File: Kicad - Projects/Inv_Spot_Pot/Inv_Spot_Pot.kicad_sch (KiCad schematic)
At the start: 72 parts, among them J1 Screw_Terminal_01x03, J2 PWM, J3 Display_Power, J4 Current_Sense, J5 PWM, Q1 40T120, Q2 40T120, Q3 40T120, Q4 40T120, T1 Transformer_1P_1S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

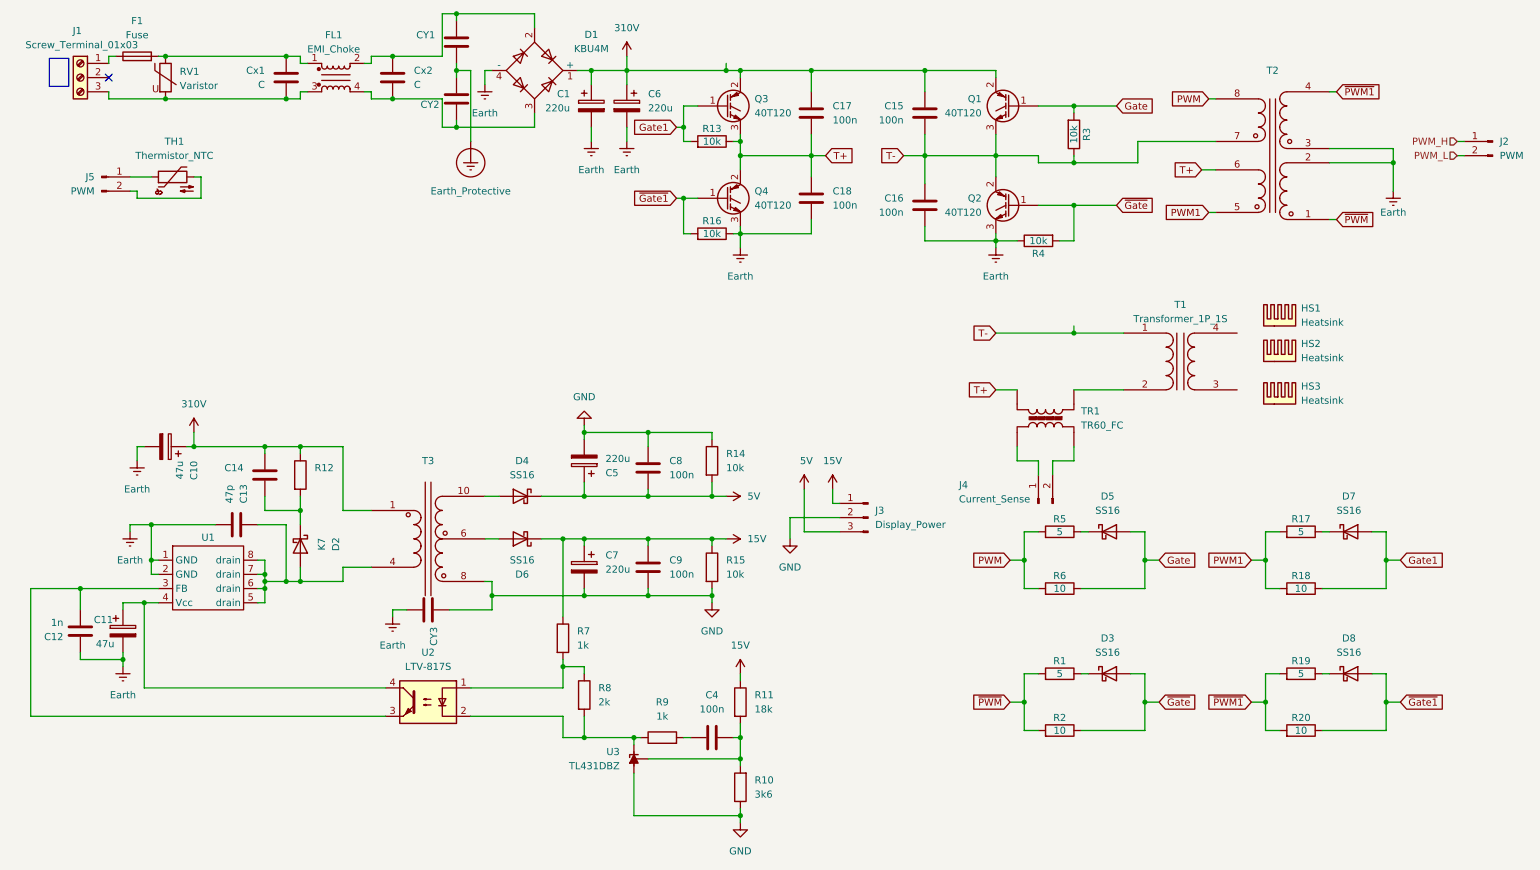
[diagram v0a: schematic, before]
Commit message: Ajustes Finais
Ajustes finais de footprints e layouts
Considerando aumentar isolamento da trilha T- do IGBT Q2
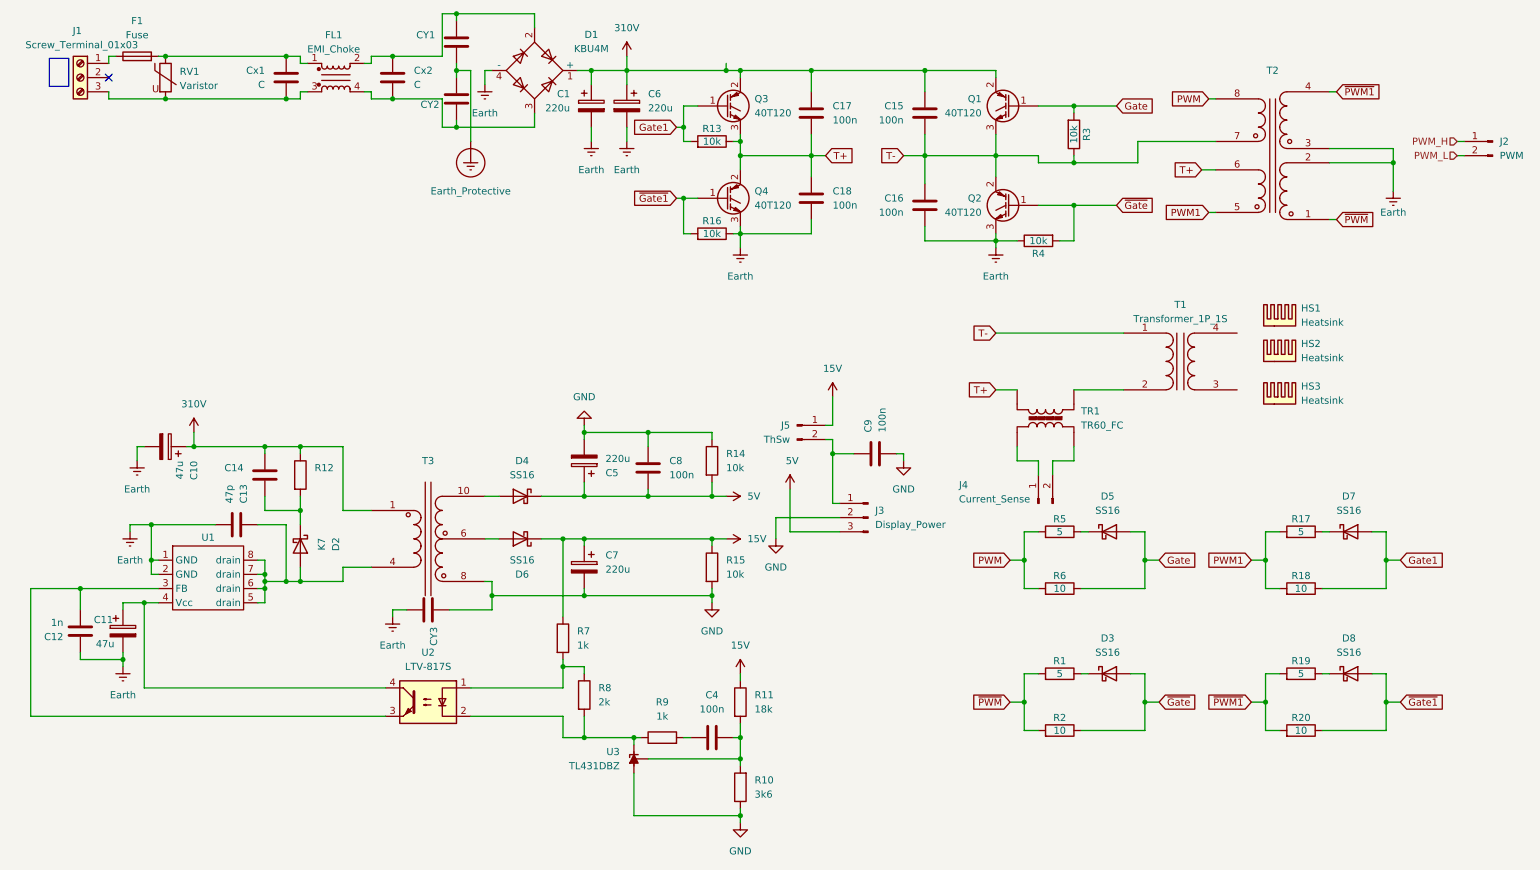
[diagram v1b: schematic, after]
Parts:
- removed TH1: Thermistor_NTC, Resistor_THT:R_Axial_DIN0204_L3.6mm_D1.6mm_P1.90mm_Vertical, symbol Device:Thermistor_NTC
- C1, C6: footprint Capacitor_THT:C_Radial_D16.0mm_H25.0mm_P7.50mm -> Capacitor_THT:CP_Radial_D35.0mm_P10.00mm_SnapIn
- J2, J4: footprint Connector_PinHeader_2.00mm:PinHeader_1x02_P2.00mm_Vertical -> Connector_PinHeader_2.54mm:PinHeader_1x02_P2.54mm_Vertical
- J3: footprint Connector_PinHeader_2.00mm:PinHeader_1x03_P2.00mm_Vertical -> Connector_PinHeader_2.54mm:PinHeader_1x03_P2.54mm_Vertical
- J5: value PWM -> ThSw; footprint Connector_PinHeader_2.00mm:PinHeader_1x02_P2.00mm_Vertical -> Connector_PinHeader_2.54mm:PinHeader_1x02_P2.54mm_Vertical
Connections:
- net 15V: now also J5.1 (Pin_1); no longer C9.1, J3.1 (Pin_1)
- net at J5.2 (Pin_2): now also C9.1, J3.1 (Pin_1)
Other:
- moved on the sheet: C9, J5

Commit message: Ajustes Finais
Ajustes Finais do código, esquemáticos e layouts

Ainda faltam ajustes finos
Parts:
- added R21: 200k, Resistor_SMD:R_1206_3216Metric_Pad1.30x1.75mm_HandSolder, symbol Device:R
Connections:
- net 310V: now also R21.1
- net Earth: now also R21.2
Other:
- moved on the sheet: C15, C16, C17, C18, J2, Q1, Q2, Q3, Q4, R13, R16, R3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

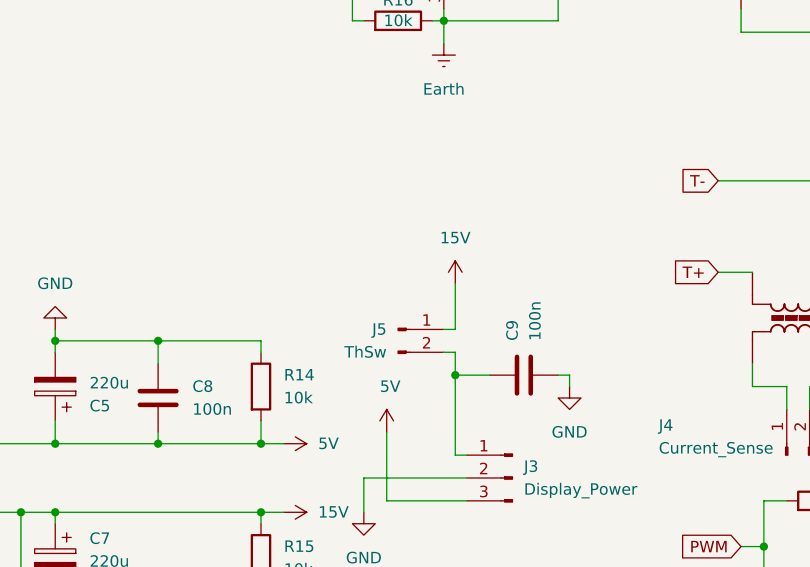
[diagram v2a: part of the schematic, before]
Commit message: Ajustes de Esquemático / Layout
Ajustado símbolo da chave bimetálica na linha de 15V para proteção térmica

Ajustada trilhas de PWM que estavam sendo cobertas por um capacitor
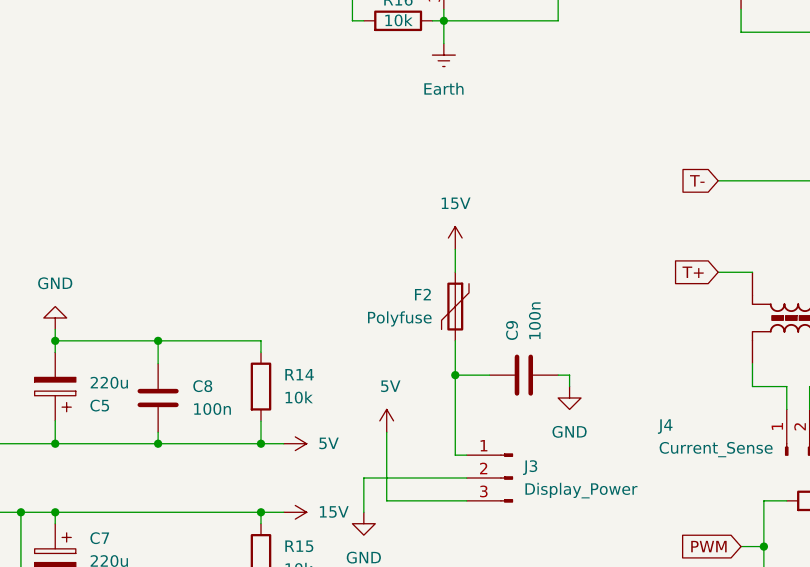
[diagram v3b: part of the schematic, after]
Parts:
- removed J5: ThSw, Connector_PinHeader_2.54mm:PinHeader_1x02_P2.54mm_Vertical, symbol Connector:Conn_01x02_Pin
- added F2: Polyfuse, Connector_PinHeader_2.54mm:PinHeader_1x02_P2.54mm_Vertical, symbol Device:Polyfuse
- F1: footprint Fuse:Fuseholder_Clip-5x20mm_Bel_FC-203-22_Lateral_P17.80x5.00mm_D1.17mm_Horizontal -> Fuse:Fuseholder_Clip-5x20mm_Schurter_CQM_Inline_P20.60x5.00mm_D1.00mm_Horizontal
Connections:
- net 15V: now also F2.1
- net at C9.1, J3.1 (Pin_1): now also F2.2
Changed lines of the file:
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@@
 	)
 	(junction
-		(at 160.02 102.87)
-		(diameter 0)
-		(color 0 0 0 0)
-	)
-	(junction
 		(at 81.28 31.75)
 		(diameter 0)
@@
 	)
 	(junction
+		(at 160.02 102.87)
+		(diameter 0)
+		(color 0 0 0 0)
+	)
+	(junction
 		(at 115.57 99.06)
 		(diameter 0)
@@
 	(wire
 		(pts
-			(xy 158.75 97.79) (xy 160.02 97.79)
-		)
-		(stroke
-			(width 0)
-			(type default)
-		)
-	)
-	(wire
-		(pts
 			(xy 127 157.48) (xy 143.51 157.48)
 		)
@@
 	(wire
 		(pts
-			(xy 160.02 100.33) (xy 160.02 102.87)
-		)
-		(stroke
-			(width 0)
-			(type default)
-		)
-	)
-	(wire
-		(pts
 			(xy 92.71 33.02) (xy 92.71 34.29)
 		)
@@
 	(wire
 		(pts
-			(xy 160.02 92.71) (xy 160.02 97.79)
+			(xy 160.02 88.9) (xy 160.02 91.44)
 		)
 		(stroke
@@
 	(wire
 		(pts
-			(xy 158.75 100.33) (xy 160.02 100.33)
-		)
-		(stroke
-			(width 0)
-			(type default)
-		)
-	)
-	(wire
-		(pts
 			(xy 204.47 49.53) (xy 204.47 53.34)
 		)
@@
 	(wire
 		(pts
+			(xy 160.02 99.06) (xy 160.02 102.87)
+		)
+		(stroke
+			(width 0)
+			(type default)
+		)
+	)
+	(wire
+		(pts
 			(xy 138.43 100.33) (xy 138.43 99.06)
 		)
@@
 	)
 	(symbol
+		(lib_id "Device:Polyfuse")
+		(at 160.02 95.25 0)
+		(mirror y)
+		(unit 1)
+		(body_style 1)
+		(exclude_from_sim no)
+		(in_bom yes)
+		(on_board yes)
+		(in_pos_files yes)
+		(dnp no)
+		(property "Reference" "F2"
+			(at 157.48 93.9799 0)
+			(show_name no)
+			(do_not_autoplace no)
+			(effects
+				(font
+					(size 1.27 1.27)
+				)
+				(justify left)
+			)
+		)
+		(property "Value" "Polyfuse"
+			(at 157.48 96.5199 0)
+			(show_name no)
+			(do_not_autoplace no)
+			(effects
+				(font
+					(size 1.27 1.27)
+				)
+				(justify left)
+			)
+		)
+		(property "Footprint" "Connector_PinHeader_2.54mm:PinHeader_1x02_P2.54mm_Vertical"
+			(at 158.75 100.33 0)
+			(hide yes)
+			(show_name no)
+			(do_not_autoplace no)
+			(effects
+				(font
+					(size 1.27 1.27)
+				)
+				(justify left)
+			)
+		)
+		(property "Datasheet" ""
+			(at 160.02 95.25 0)
+			(hide yes)
+			(show_name no)
+			(do_not_autoplace no)
+			(effects
+				(font
+					(size 1.27 1.27)
+				)
+			)
+		)
+		(property "Description" "Resettable fuse, polymeric positive temperature coefficient"
+			(at 160.02 95.25 0)
+			(hide yes)
+			(show_name no)
+			(do_not_autoplace no)
+			(effects
+				(font
+					(size 1.27 1.27)
+				)
+			)
+		)
+		(pin "1"
+		)
+		(pin "2"
+		)
+		(instances
+			(project "Inv_Spot_Pot"
+				(path "/e27abe51-96c0-4fdf-ba00-b5a281cd0e9c"
+					(reference "F2")
+					(unit 1)
+				)
+			)
+		)
+	)
+	(symbol
 		(lib_id "Device:C")
 		(at 81.28 35.56 0)
@@
 			)
 		)
-		(property "Footprint" "Fuse:Fuseholder_Clip-5x20mm_Bel_FC-203-22_Lateral_P17.80x5.00mm_D1.17mm_Horizontal"
+		(property "Footprint" "Fuse:Fuseholder_Clip-5x20mm_Schurter_CQM_Inline_P20.60x5.00mm_D1.00mm_Horizontal"
 			(at 35.56 33.528 90)
 			(hide yes)
@@
 	(symbol
 		(lib_id "power:VCC")
-		(at 160.02 92.71 0)
+		(at 160.02 88.9 0)
 		(unit 1)
 		(body_style 1)
@@
 		(fields_autoplaced yes)
 		(property "Reference" "#PWR018"
-			(at 160.02 96.52 0)
+			(at 160.02 92.71 0)
 			(hide yes)
 			(show_name no)
@@
 		)
 		(property "Value" "15V"
-			(at 160.02 87.63 0)
+			(at 160.02 83.82 0)
 			(show_name no)
 			(do_not_autoplace no)
@@
 		)
 		(property "Footprint" ""
-			(at 160.02 92.71 0)
+			(at 160.02 88.9 0)
 			(hide yes)
 			(show_name no)
@@
 		)
 		(property "Datasheet" ""
-			(at 160.02 92.71 0)
+			(at 160.02 88.9 0)
 			(hide yes)
 			(show_name no)
@@
 		)
 		(property "Description" "Power symbol creates a global label with name \"VCC\""
-			(at 160.02 92.71 0)
+			(at 160.02 88.9 0)
 			(hide yes)
 			(show_name no)
@@
 					(unit 1)
 				)
-			)
-		)
-	)
-	(symbol
-		(lib_id "Connector:Conn_01x02_Pin")
-		(at 153.67 97.79 0)
-		(unit 1)
-		(body_style 1)
-		(exclude_from_sim no)
-		(in_bom yes)
-		(on_board yes)
-		(in_pos_files yes)
-		(dnp no)
-		(property "Reference" "J5"
-			(at 152.4 97.7899 0)
-			(show_name no)
-			(do_not_autoplace no)
-			(effects
-				(font
-					(size 1.27 1.27)
-				)
-				(justify right)
-			)
-		)
-		(property "Value" "ThSw"
-			(at 152.4 100.3299 0)
-			(show_name no)
-			(do_not_autoplace no)
-			(effects
-				(font
-					(size 1.27 1.27)
-				)
-				(justify right)
-			)
-		)
-		(property "Footprint" "Connector_PinHeader_2.54mm:PinHeader_1x02_P2.54mm_Vertical"
-			(at 153.67 97.79 0)
-			(hide yes)
-			(show_name no)
-			(do_not_autoplace no)
-			(effects
-				(font
-					(size 1.27 1.27)
-				)
-			)
-		)
-		(property "Datasheet" ""
-			(at 153.67 97.79 0)
-			(hide yes)
-			(show_name no)
-			(do_not_autoplace no)
-			(effects
-				(font
-					(size 1.27 1.27)
-				)
-			)
-		)
-		(property "Description" "Generic connector, single row, 01x02, script generated"
-			(at 153.67 97.79 0)
-			(hide yes)
-			(show_name no)
-			(do_not_autoplace no)
-			(effects
-				(font
-					(size 1.27 1.27)
-				)
-			)
-		)
-		(pin "2"
-		)
-		(pin "1"
-		)
-		(instances
-			(project "Inv_Spot_Pot"
-				(path "/e27abe51-96c0-4fdf-ba00-b5a281cd0e9c"
-					(reference "J5")
-					(unit 1)
-				)

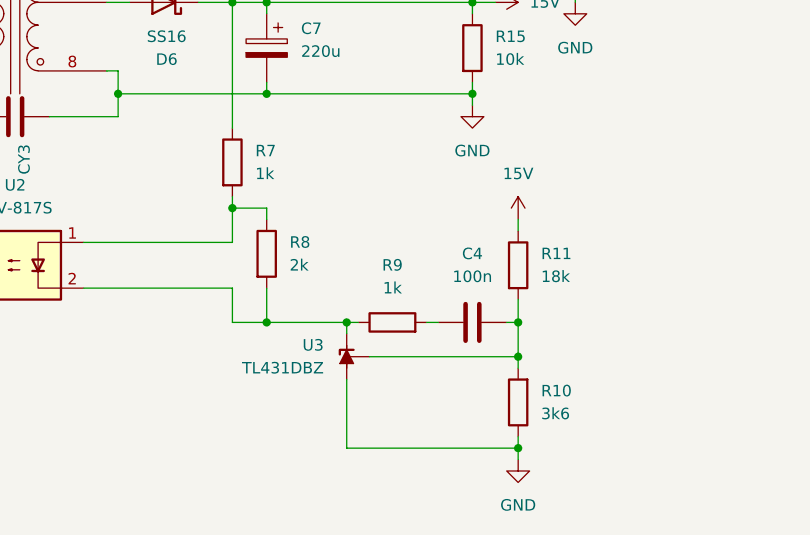
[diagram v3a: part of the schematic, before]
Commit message: Melhora no Acionamento do Trigger
Acionamento do trigger agora ocorre quando o circuito é fechado, não aberto.

Adição de vias de GND na saída da fonte auxiliar.
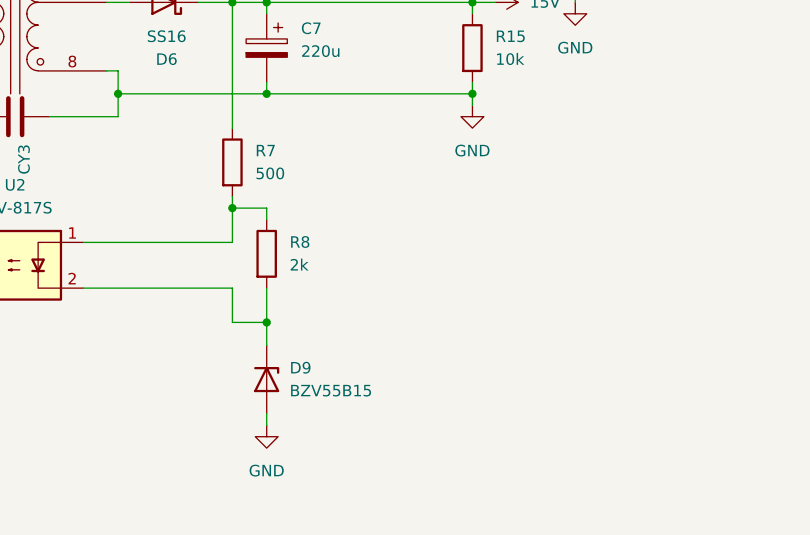
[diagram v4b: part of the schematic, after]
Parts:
- removed C4: 100n, Capacitor_SMD:C_1206_3216Metric_Pad1.33x1.80mm_HandSolder, symbol Device:C
- removed R10: 3k6, Resistor_SMD:R_1206_3216Metric_Pad1.30x1.75mm_HandSolder, symbol Device:R
- removed R11: 18k, Resistor_SMD:R_1206_3216Metric_Pad1.30x1.75mm_HandSolder, symbol Device:R
- removed R9: 1k, Resistor_SMD:R_1206_3216Metric_Pad1.30x1.75mm_HandSolder, symbol Device:R
- removed U3: TL431DBZ, Package_TO_SOT_SMD:SOT-23_Handsoldering, symbol Reference_Voltage:TL431DBZ
- added D9: BZV55B15, Diode_SMD:D_MiniMELF, symbol Diode:BZV55B15
- R7: value 1k -> 500
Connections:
- net GND: now also D9.2 (A)
- net at R8.2, U2.2: now also D9.1 (K)
